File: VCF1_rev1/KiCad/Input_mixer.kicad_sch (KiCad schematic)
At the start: 30 parts, among them J1 AudioJack2_SwitchT, J2 AudioJack2_SwitchT, J3 AudioJack2_SwitchT, Q1 Q_NPN_BCE, U5 Opamp_Quad

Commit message: A lot of work especially on VCF2. Doc updated. Schematics a bit in a flux due to major restructuring.
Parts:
- removed C20, C21: 100nF, symbol Device:C
- removed unit 5 of U5
- renumbered C17 to C14, C18 to C15, C19 to C16, C22 to C19, D1 to D4, D2 to D5, D3 to D6, D4 to D7, D5 to D8, D6 to D9, R33 to R39, R34 to R40, R35 to R41, R36 to R42, R37 to R43, R38 to R44, R39 to R45, R40 to R46, R41 to R47, R42 to R48, R43 to R49, U5 to U7

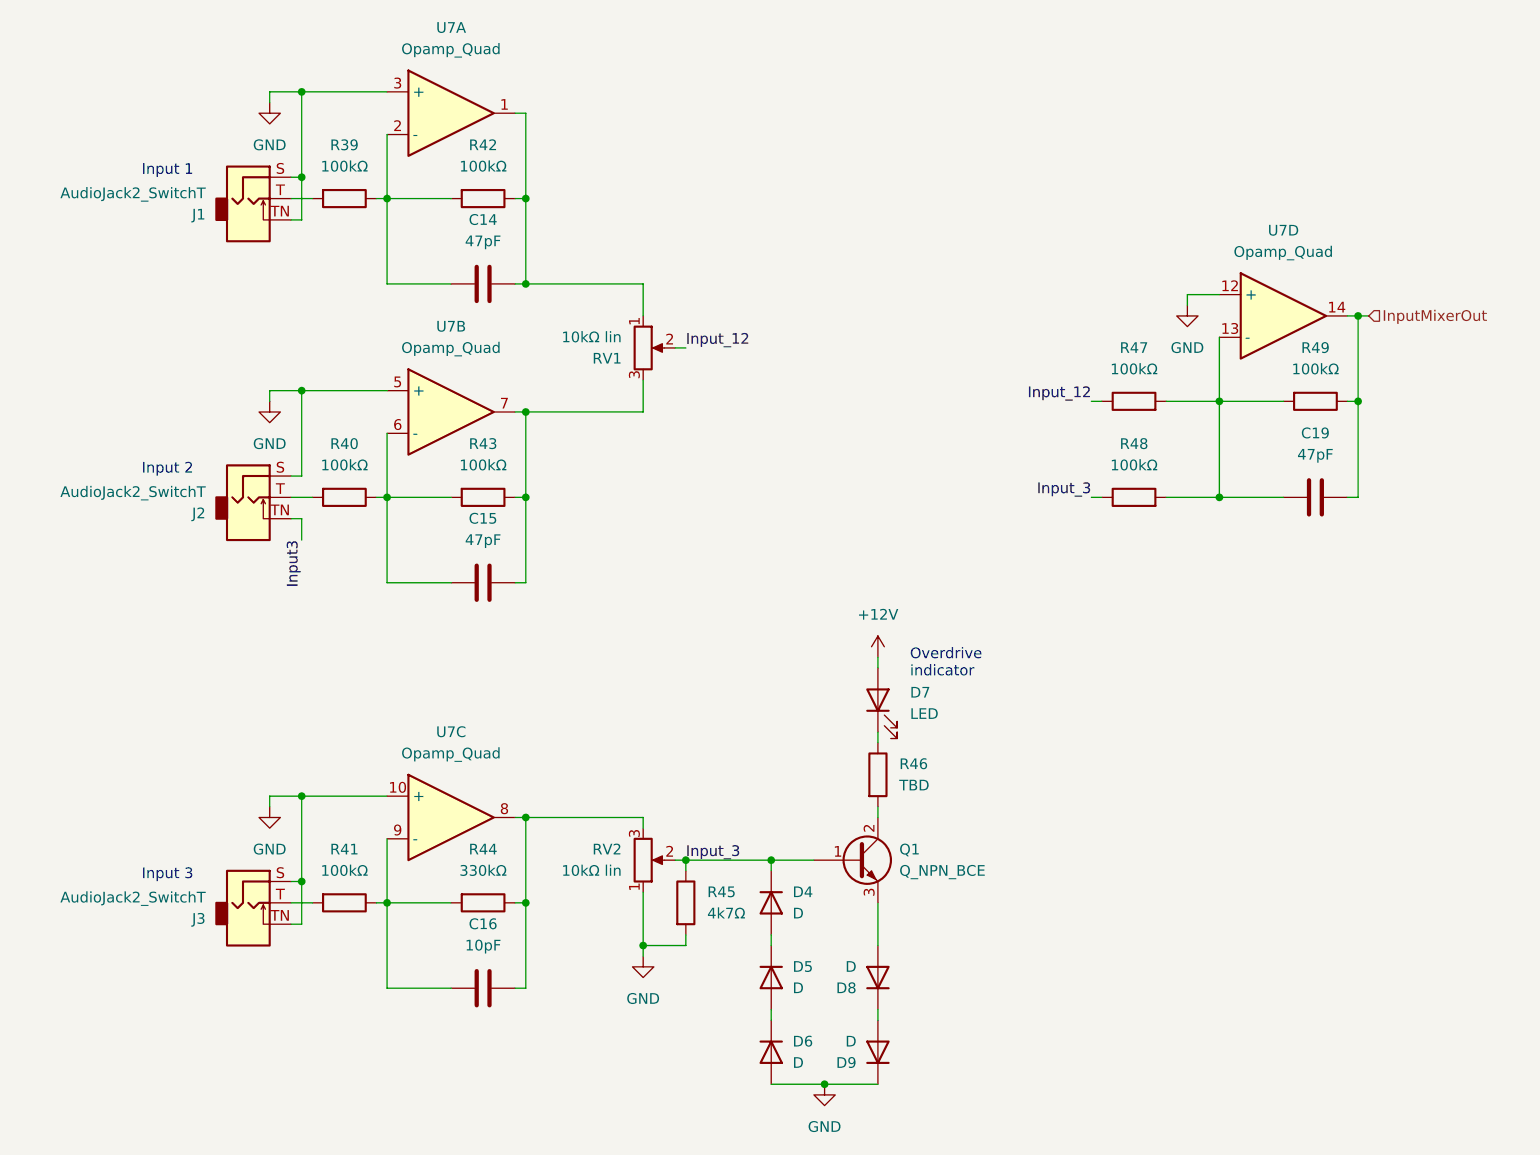
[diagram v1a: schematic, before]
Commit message: Added VCA (with a quirk) and also drew a new symbol for 74HC4053 because the standard one annoyed me.
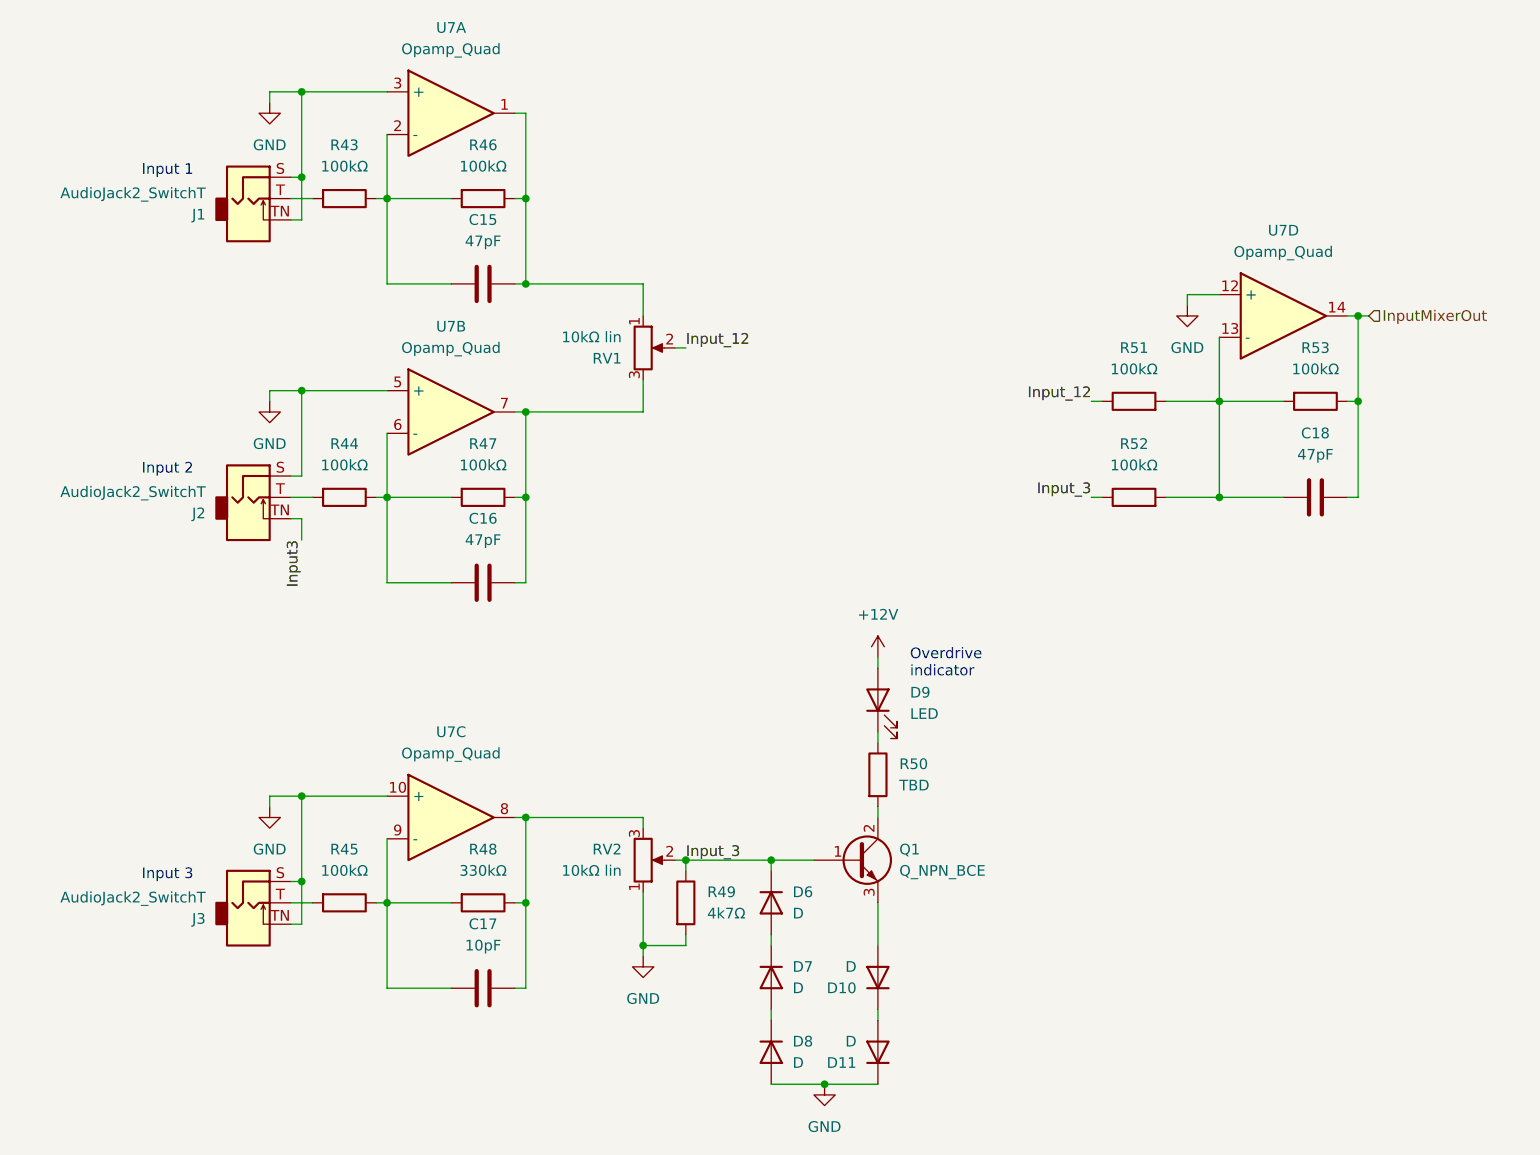
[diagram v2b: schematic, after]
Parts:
- renumbered C14 to C15, C15 to C16, C16 to C17, C19 to C18, D8 to D10, D9 to D11, D4 to D6, D5 to D7, D6 to D8, D7 to D9, R39 to R43, R40 to R44, R41 to R45, R42 to R46, R43 to R47, R44 to R48, R45 to R49, R46 to R50, R47 to R51, R48 to R52, R49 to R53

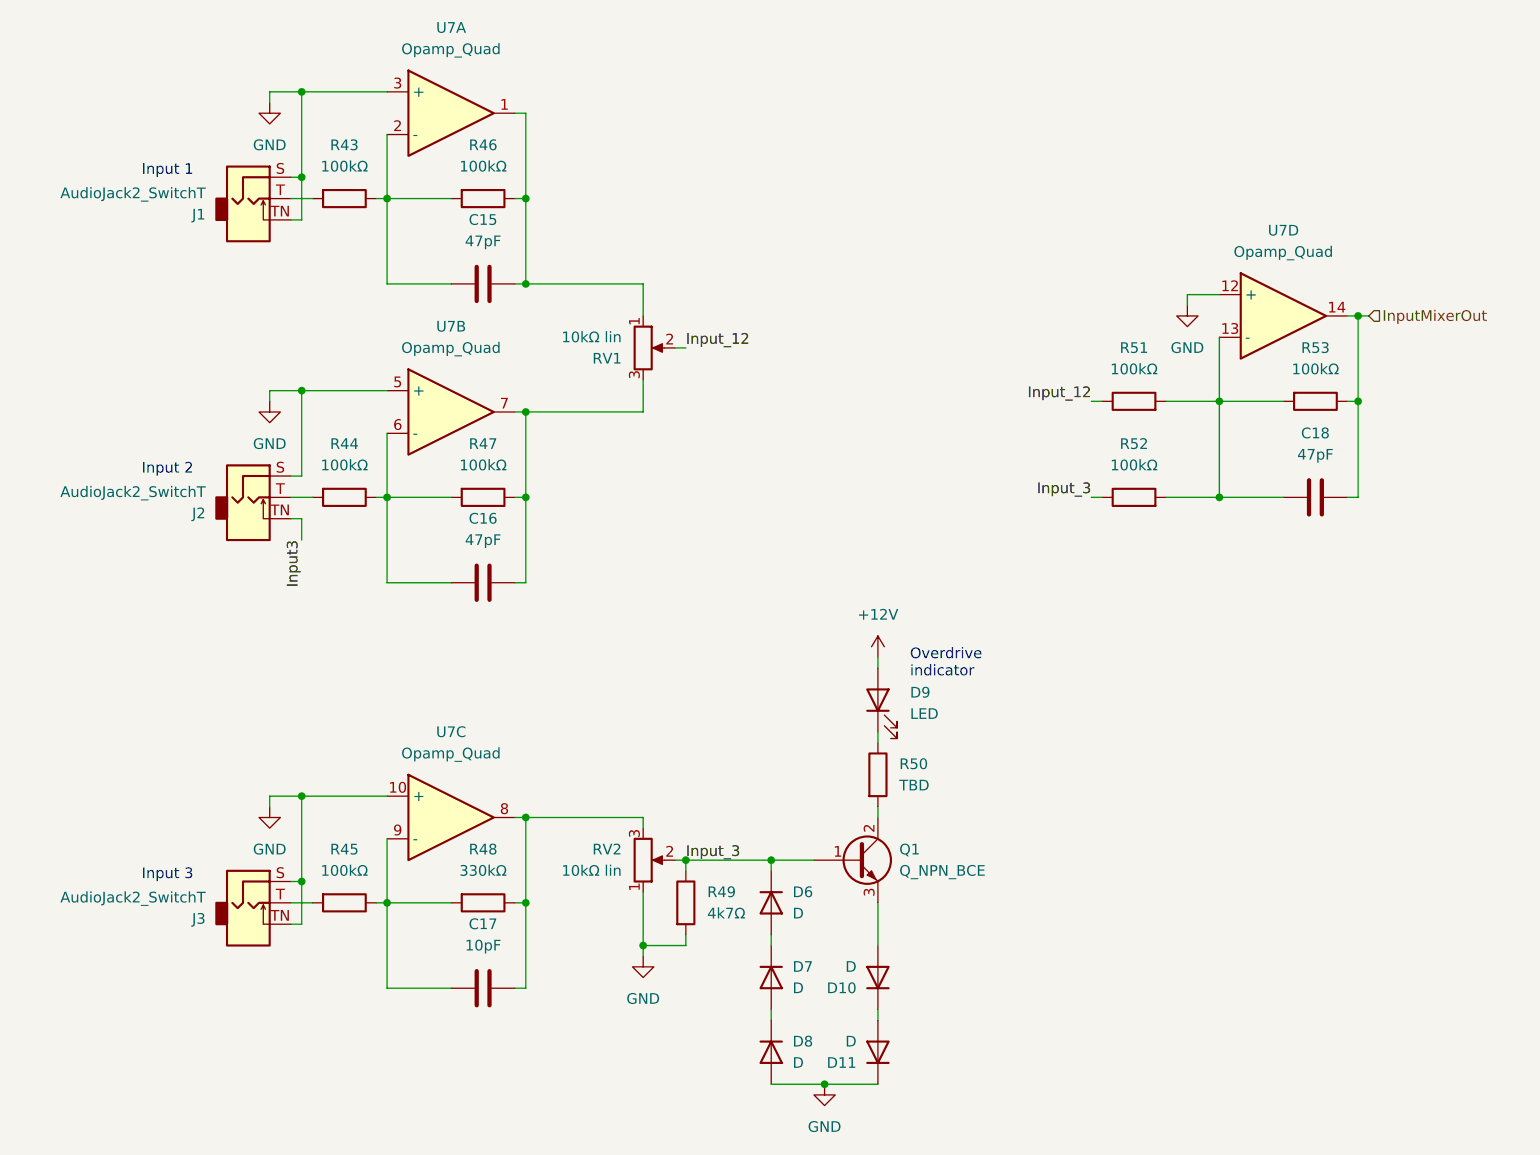
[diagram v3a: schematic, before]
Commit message: The filter blocks are more or less done, page order has gotten more sane for easier reading.
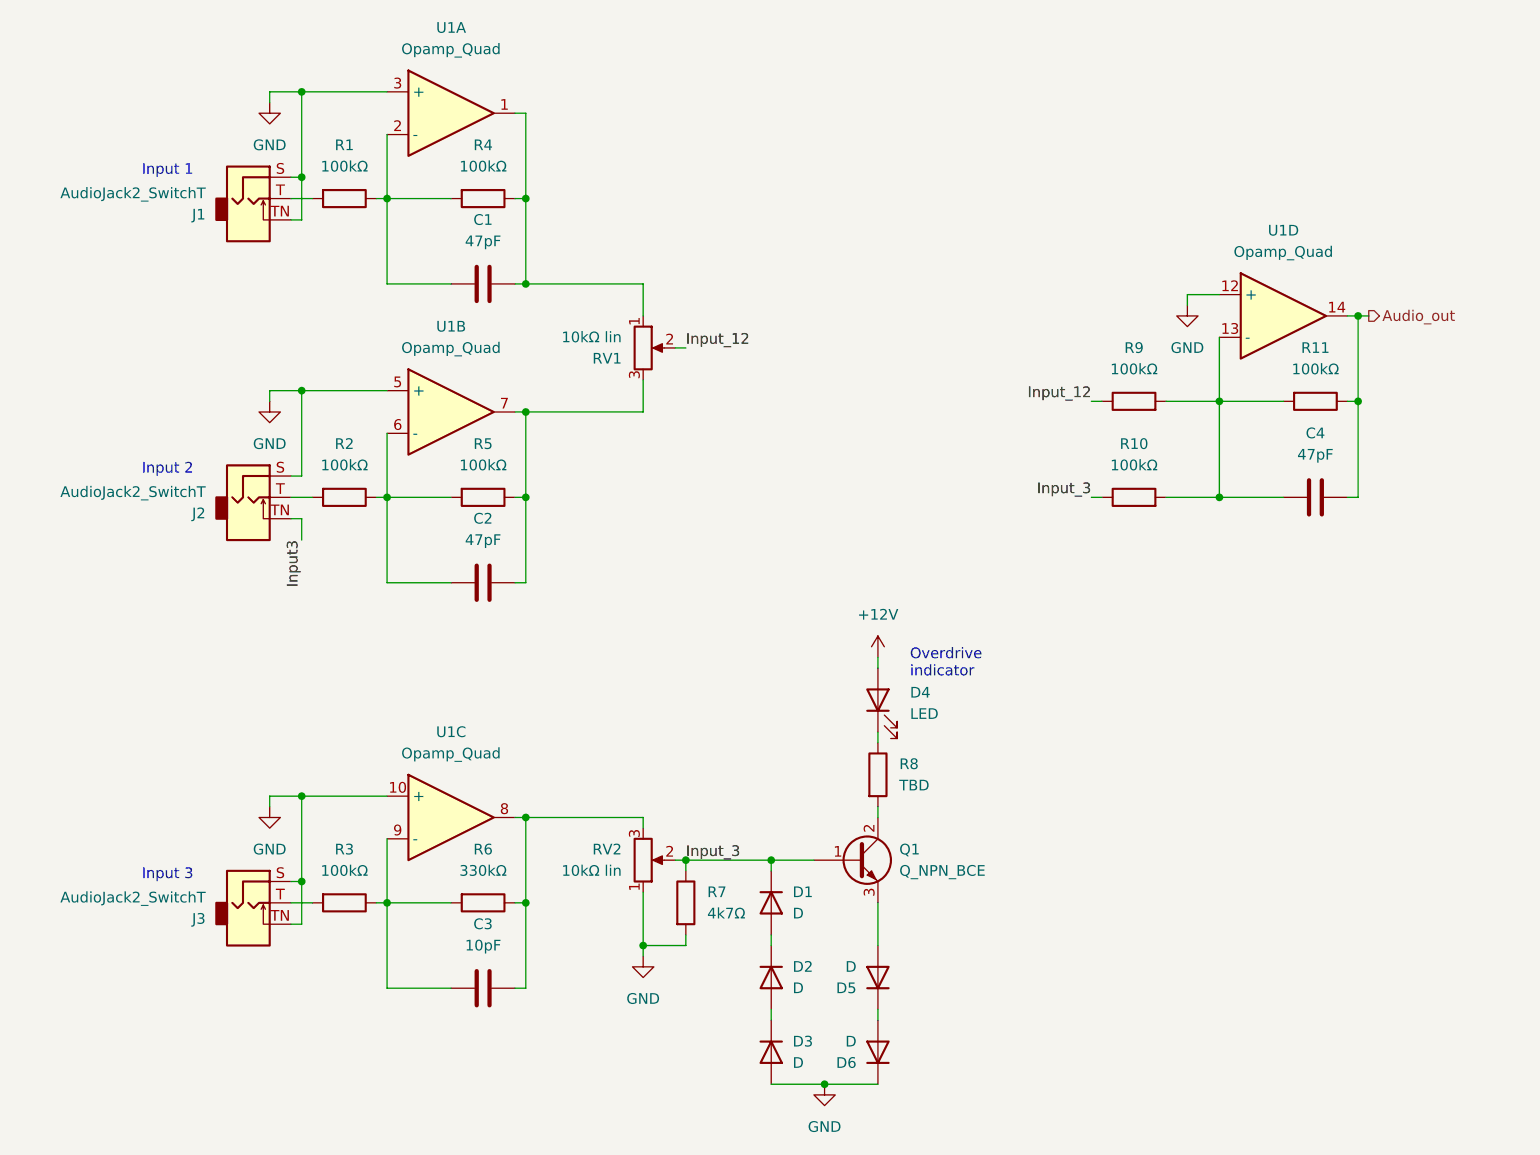
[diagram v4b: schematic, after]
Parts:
- renumbered C15 to C1, C16 to C2, C17 to C3, C18 to C4, D6 to D1, D7 to D2, D8 to D3, D9 to D4, D10 to D5, D11 to D6, R43 to R1, R52 to R10, R53 to R11, R44 to R2, R45 to R3, R46 to R4, R47 to R5, R48 to R6, R49 to R7, R50 to R8, R51 to R9, U7 to U1
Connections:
- net InputMixerOut renamed Audio_out

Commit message: Lot of work on panel etc.
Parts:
- renumbered J1 to J2, J2 to J3, J3 to J4, R1 to R13, R2 to R14, R3 to R15, R4 to R16, R5 to R17, R6 to R18, R7 to R19, R8 to R20, R9 to R21, R10 to R22, R11 to R23, RV1 to RV6, RV2 to RV7
